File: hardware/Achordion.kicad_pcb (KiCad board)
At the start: 2 copper layers, 44.5 x 109.4 mm, 96 parts, among them J1 Power, J10 Jack, J11 Jack, J4 Jack, J5 Jack, J6 Jack, J7 Jack, J8 Jack, J9 Jack, SW2 Button, U4 LM4040C10, U6 TL072, U7 MCP6002, U8 MCP6002, U9 MCP6002

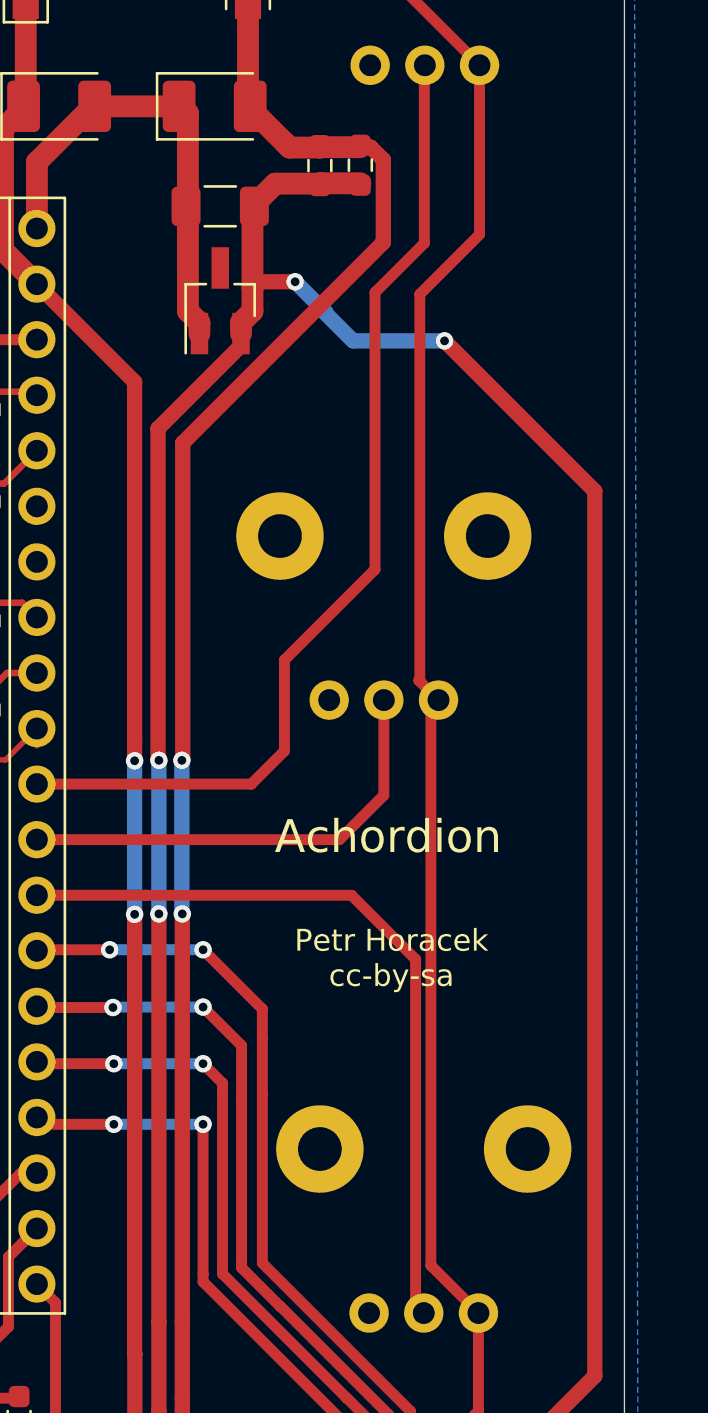
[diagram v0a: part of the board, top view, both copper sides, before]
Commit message: Add graphics to the PCB
Make it look more interesting.

Signed-off-by: Petr Horacek <hrck@protonmail.com>
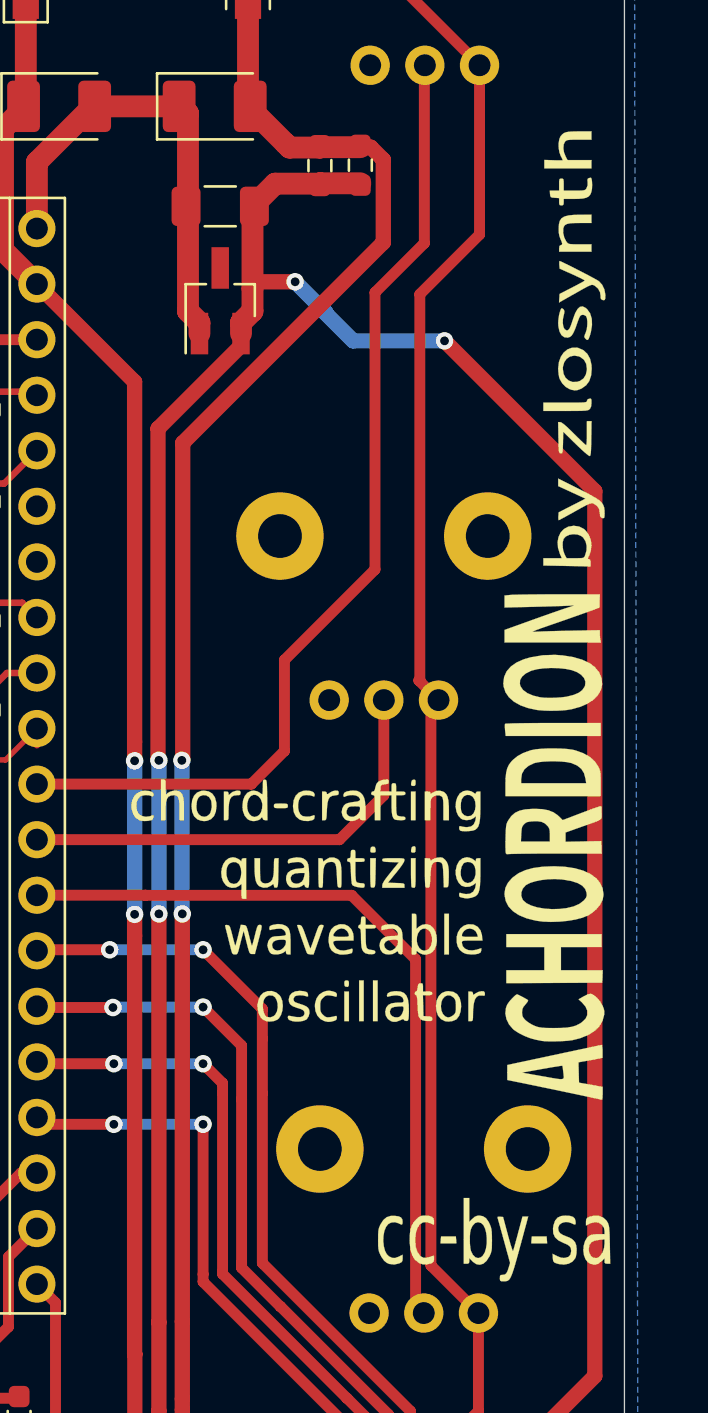
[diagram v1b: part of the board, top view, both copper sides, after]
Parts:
- added G***: LOGO, Graphics:Graphics_Back, B.Cu at (148.3, 105.9)
- added G***: LOGO, Graphics:Graphics_Front, F.Cu at (155.7, 86.4)
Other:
- board text removed: "Achordion"
- board text removed: "Petr Horacek cc-by-sa"

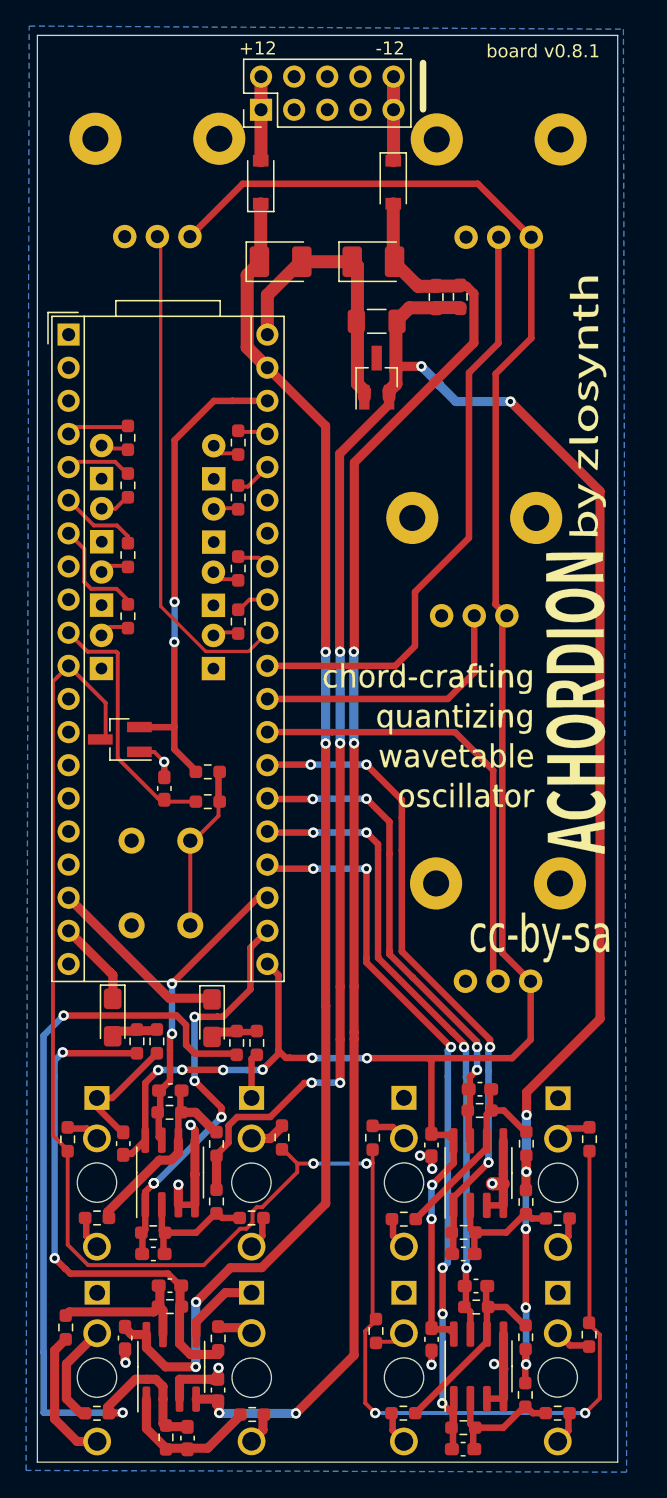
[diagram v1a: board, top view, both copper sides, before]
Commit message: Widen tracks on the PCB
Where possible, make them at least 0.5 mm wide.

Signed-off-by: Petr Horacek <hrck@protonmail.com>
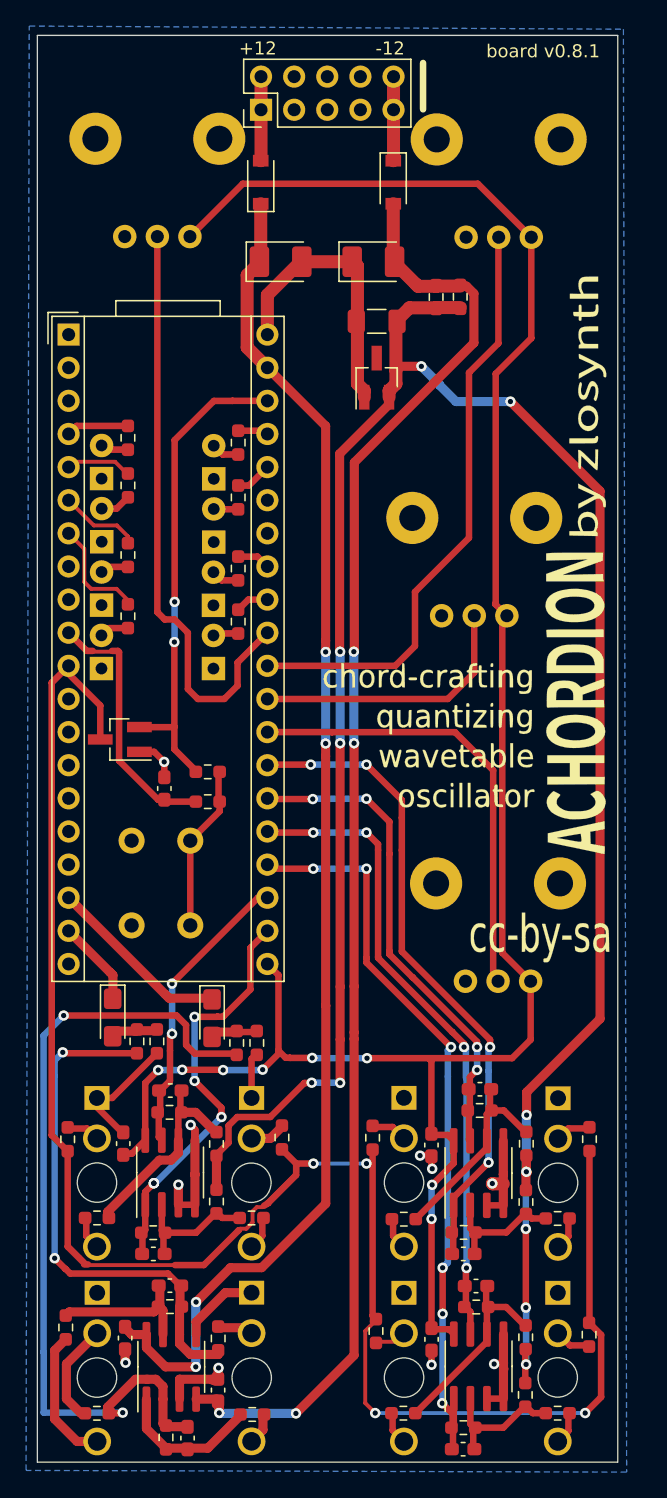
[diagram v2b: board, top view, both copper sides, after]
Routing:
- net PROBE: track 140.7 -> 229.5 mm
- net BUTTON: track 20.0 -> 30.5 mm
- net POT2: track 39.4 -> 46.8 mm
- net LED5: track 4.77 -> 9.57 mm
- net LED2: track 2.86 -> 5.68 mm
- net LED4: track 2.59 -> 5.15 mm
- net LED3: track 2.51 -> 5.07 mm
- net Net-(D8-Pad2): track 2.42 -> 4.78 mm
- net LED1: track 2.30 -> 4.64 mm
- net Net-(D10-Pad2): track 2.30 -> 4.56 mm
- net GND: track 78.5 -> 80.7 mm
- net Net-(D9-Pad2): track 2.22 -> 4.40 mm
- net Net-(D5-Pad2): track 2.12 -> 4.28 mm
- net Net-(D3-Pad2): track 2.12 -> 4.28 mm
- net Net-(D7-Pad2): track 2.12 -> 4.27 mm
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
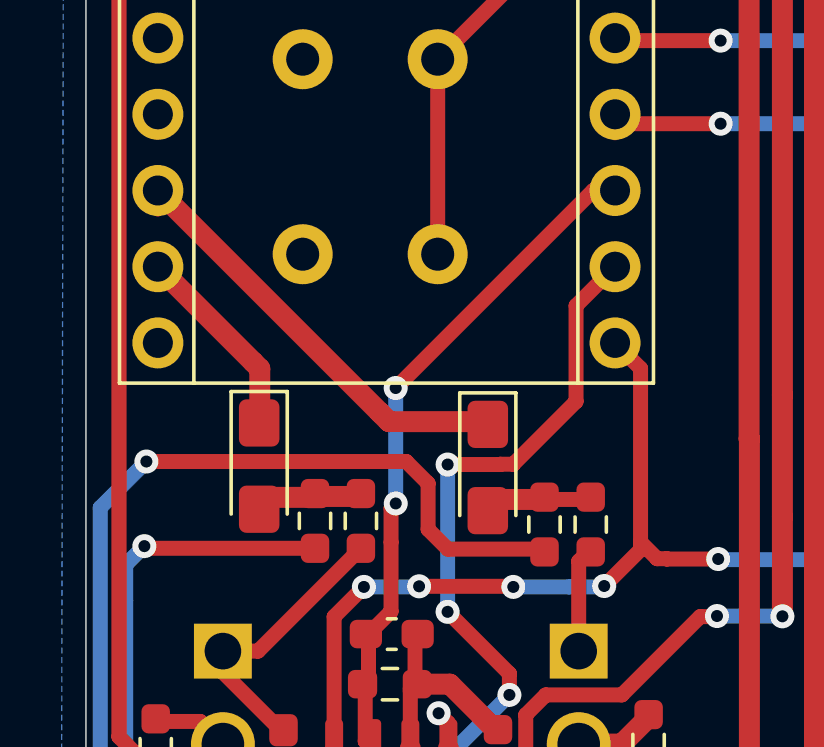
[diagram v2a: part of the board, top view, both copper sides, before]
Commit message: Replace DAC decoupling cap with LPF
The design with big decoupling cap was taken from WM8731 used for
Elements. However, with AK4556 used in Daisy Seed, it is not needed (or
at least not a part of the datasheet), instead, use LPF for ~70 kHz.

Signed-off-by: Petr Horacek <hrck@protonmail.com>
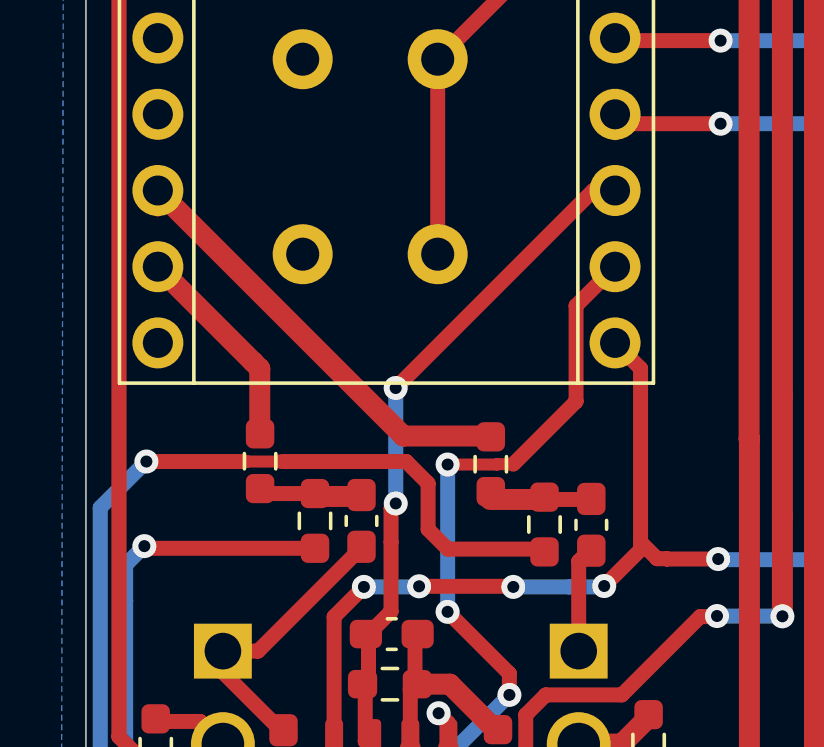
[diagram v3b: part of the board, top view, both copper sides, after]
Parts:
- C35, C37: value 10u -> 1n; footprint Capacitor_Tantalum_SMD:CP_EIA-3216-18_Kemet-A_Pad1.58x1.35mm_HandSolder -> Capacitor_SMD:C_0603_1608Metric_Pad1.08x0.95mm_HandSolder
- R11, R7: value 47k -> 2k2
- moved C35 3.94 mm to (139.7, 118.8)
- moved R11 3.91 mm to (128.6, 116.7)
- moved R7 3.89 mm to (136.3, 116.8)
- moved C37 3.87 mm to (132.0, 118.7)
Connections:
- C35 pad 1: DAC1 -> Net-(C35-Pad1)
- C35 pad 2: Net-(C35-Pad2) -> GND
- C37 pad 1: DAC2 -> Net-(C37-Pad1)
- C37 pad 2: Net-(C37-Pad2) -> GND
- R11 pad 1: Net-(C37-Pad2) -> DAC2
- R11 pad 2: GND -> Net-(C37-Pad1)
- R12 pad 1: Net-(C37-Pad2) -> Net-(C37-Pad1)
- R7 pad 1: Net-(C35-Pad2) -> DAC1
- R7 pad 2: GND -> Net-(C35-Pad1)
- R8 pad 1: Net-(C35-Pad2) -> Net-(C35-Pad1)
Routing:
- net Net-(C37-Pad2): track 3.88 -> 0.00 mm
- net Net-(C37-Pad1): track 0.00 -> 3.61 mm
- net Net-(C35-Pad2): track 3.54 -> 0.00 mm
- net Net-(C35-Pad1): track 0.00 -> 3.40 mm
- net DAC1: track 15.6 -> 16.1 mm

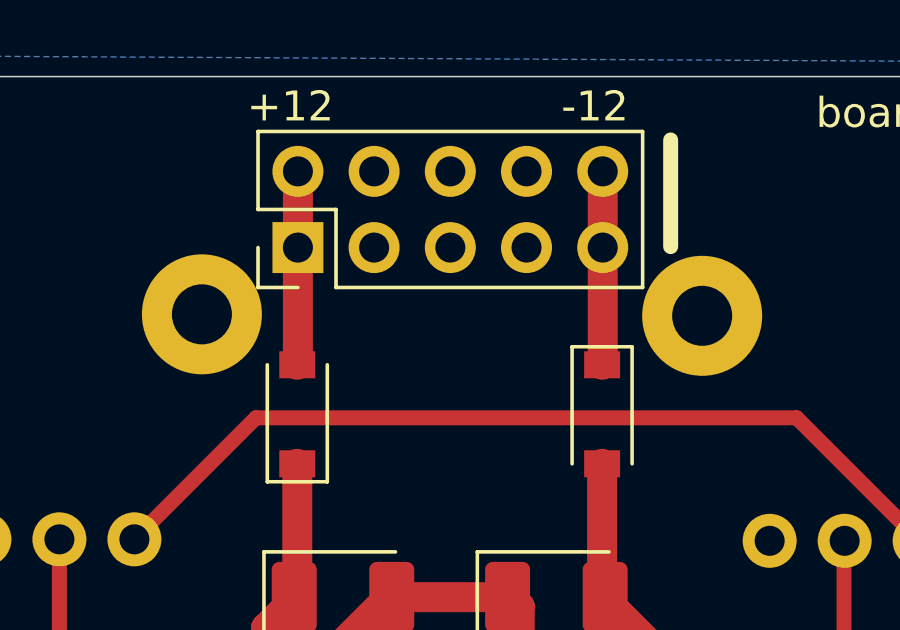
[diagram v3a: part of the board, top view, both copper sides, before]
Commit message: Add ferrite bead to filter power input
Signed-off-by: Petr Horacek <hrck@protonmail.com>
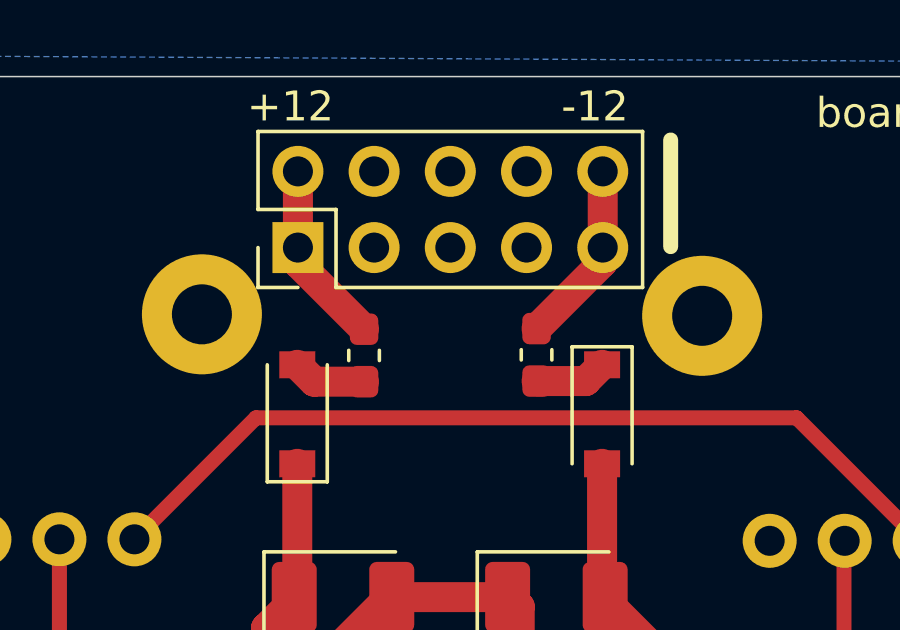
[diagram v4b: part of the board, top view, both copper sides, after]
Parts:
- added FB1: Ferrite_Bead_Small, Inductor_SMD:L_0603_1608Metric_Pad1.05x0.95mm_HandSolder, F.Cu at (142.2, 50.9)
- added FB2: Ferrite_Bead_Small, Inductor_SMD:L_0603_1608Metric_Pad1.05x0.95mm_HandSolder, F.Cu at (147.9, 50.9)
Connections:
- J1 pad 1: Net-(D1-Pad2) -> Net-(FB1-Pad2)
- J1 pad 10: Net-(D2-Pad1) -> Net-(FB2-Pad2)
- J1 pad 2: Net-(D1-Pad2) -> Net-(FB1-Pad2)
- J1 pad 9: Net-(D2-Pad1) -> Net-(FB2-Pad2)
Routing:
- net Net-(FB1-Pad2): track 0.00 -> 6.17 mm
- net Net-(FB2-Pad2): track 0.00 -> 6.15 mm
- net Net-(D2-Pad1): track 6.46 -> 2.41 mm
- net Net-(D1-Pad2): track 6.46 -> 2.46 mm

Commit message: Release version 0.9.0
Signed-off-by: Petr Horacek <hrck@protonmail.com>
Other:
- board text added: "board v0.9.0"
- board text removed: "board v0.8.1"
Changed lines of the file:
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@@
   (gr_circle (center 162.726001 144.48) (end 164.237002 144.48) (layer Edge.Cuts) (width 0.1))
   (gr_circle (center 139.236001 129.55) (end 140.747002 129.55) (layer Edge.Cuts) (width 0.1))
-  (gr_text "board v0.8.1" (at 157.24 42.79) (layer F.SilkS)
+  (gr_text "board v0.9.0" (at 157.24 42.79) (layer F.SilkS)
     (effects (font (size 1 1) (thickness 0.15)) (justify left))
   )

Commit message: Align user labels on the PCB schema
With this, labels and outlines can be printed to help with soldering.

Signed-off-by: Petr Horacek <hrck@protonmail.com>
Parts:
- D1, D2: value D_Schottky_Small -> Schottky

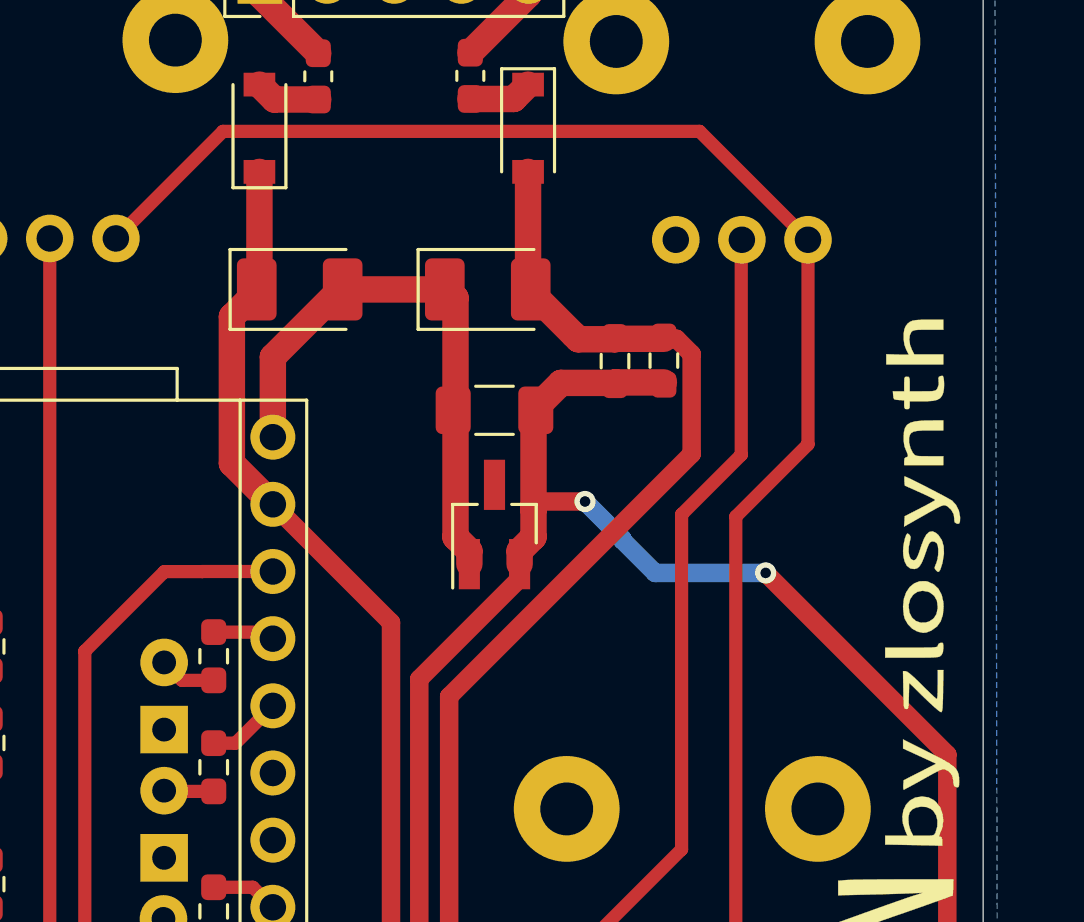
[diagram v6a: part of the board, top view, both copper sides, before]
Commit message: Replace tantalum DC decoupling caps with aluminium
Tantalum has some bad stories connected with it. This patch replaces
them with bigger, but much more common aluminium capacitors.

Signed-off-by: Petr Horacek <hrck@protonmail.com>
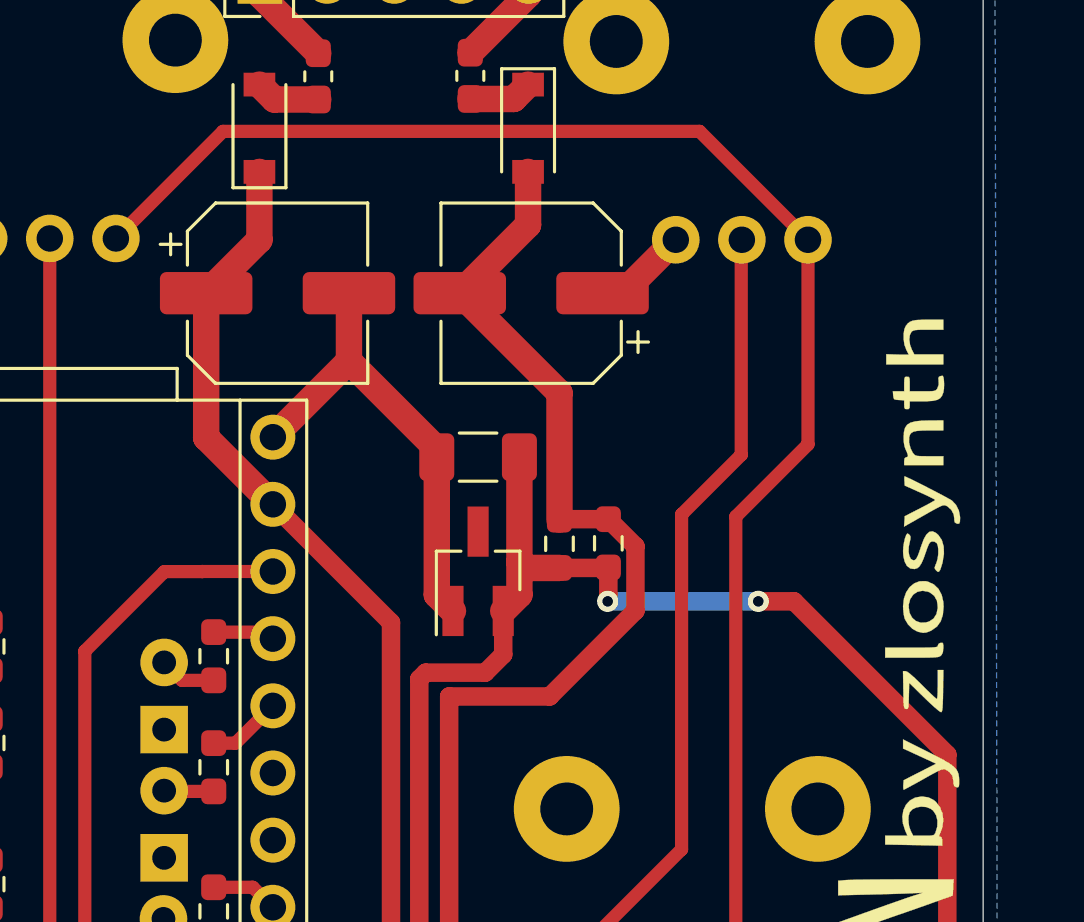
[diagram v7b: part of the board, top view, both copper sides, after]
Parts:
- C19, C20: footprint Capacitor_Tantalum_SMD:CP_EIA-3528-21_Kemet-B_Pad1.50x2.35mm_HandSolder -> Capacitor_SMD:CP_Elec_6.3x5.8
- moved R4 7.22 mm to (151.3, 68.5)
- moved R5 7.22 mm to (153.2, 68.5)
- moved C21 1.88 mm to (148.2, 65.3)
- moved U4 1.88 mm to (148.2, 69.6)
- moved C20 1.65 mm to (150.2, 59.1), turned to 180 degrees
- moved C19 0.85 mm to (140.6, 59.1)
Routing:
- net -10V: track 176.0 -> 170.0 mm
- net VEE: track 112.4 -> 114.4 mm
- net VCC: track 104.9 -> 105.7 mm

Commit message: Use 10uF for decoupling caps
This value seems to be more common in stores. It should not matter if 22
or 10 is used, so let's go with the common one.

Signed-off-by: Petr Horacek <hrck@protonmail.com>
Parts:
- C19, C20: value 22u -> 10u
